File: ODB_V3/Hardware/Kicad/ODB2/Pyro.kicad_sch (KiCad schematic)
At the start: 57 parts, among them J1 1715310000, J7 1715250000, J8 1715310000, J9 1715250000, U11 SI5442DU-T1-GE3, U12 SI5442DU-T1-GE3, U2 LM339, U3 SI5442DU-T1-GE3, U8 SI5442DU-T1-GE3

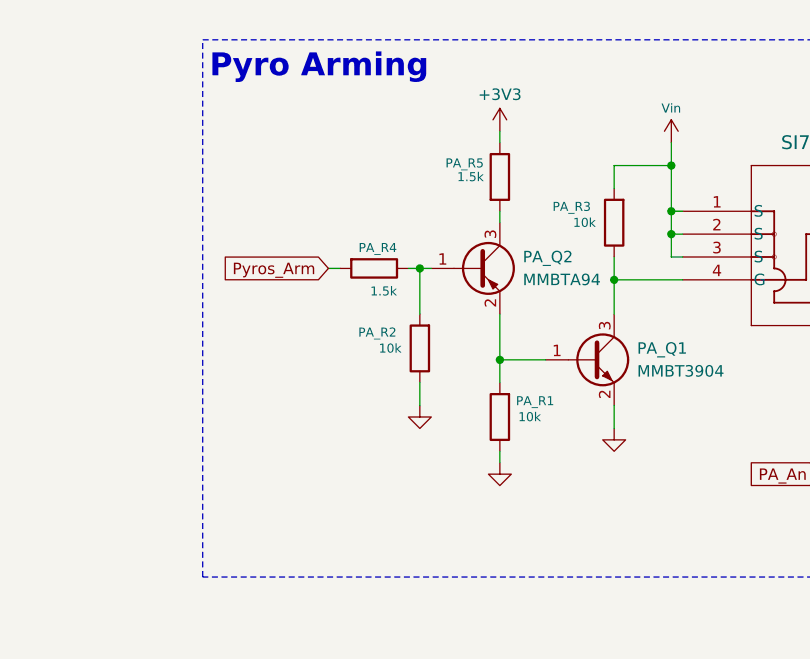
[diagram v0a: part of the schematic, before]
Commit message: WIP : Layout brouillon complet, fix pyro armement
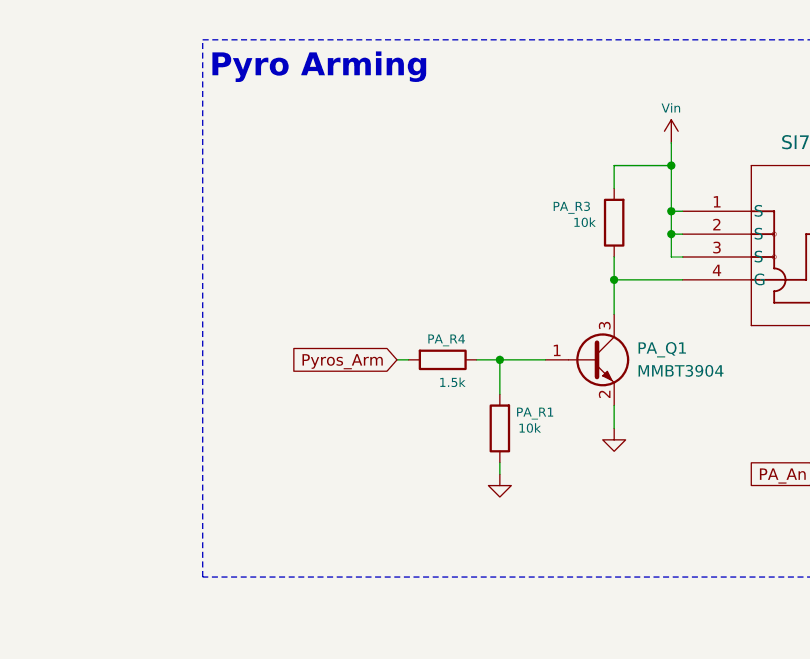
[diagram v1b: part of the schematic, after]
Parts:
- removed PA_Q2: MMBTA94, Package_TO_SOT_SMD:SOT-23, symbol Transistor_BJT:MMBTA94
- removed PA_R2: 10k, Resistor_SMD:R_0603_1608Metric, symbol Device:R
- removed PA_R5: 1.5k, Resistor_SMD:R_0603_1608Metric, symbol Device:R
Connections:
- net at PA_Q1.1 (B), PA_R1.2: now also PA_R4.1
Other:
- moved on the sheet: PA_R1, PA_R4

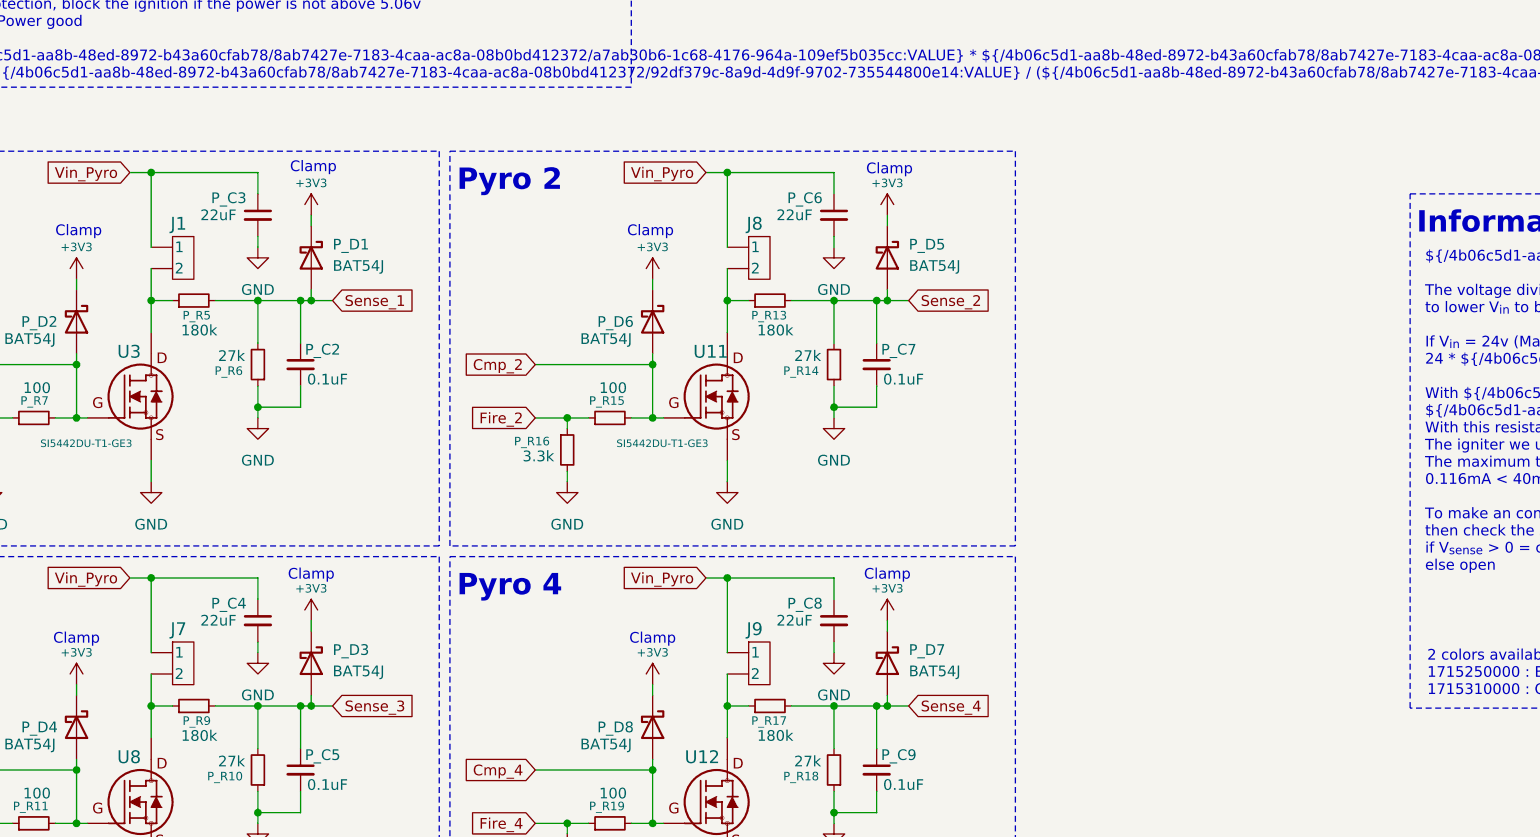
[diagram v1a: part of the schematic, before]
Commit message: WIP : Add GPIO extend, replace 5mm terminal with 2.54mm, densify layout
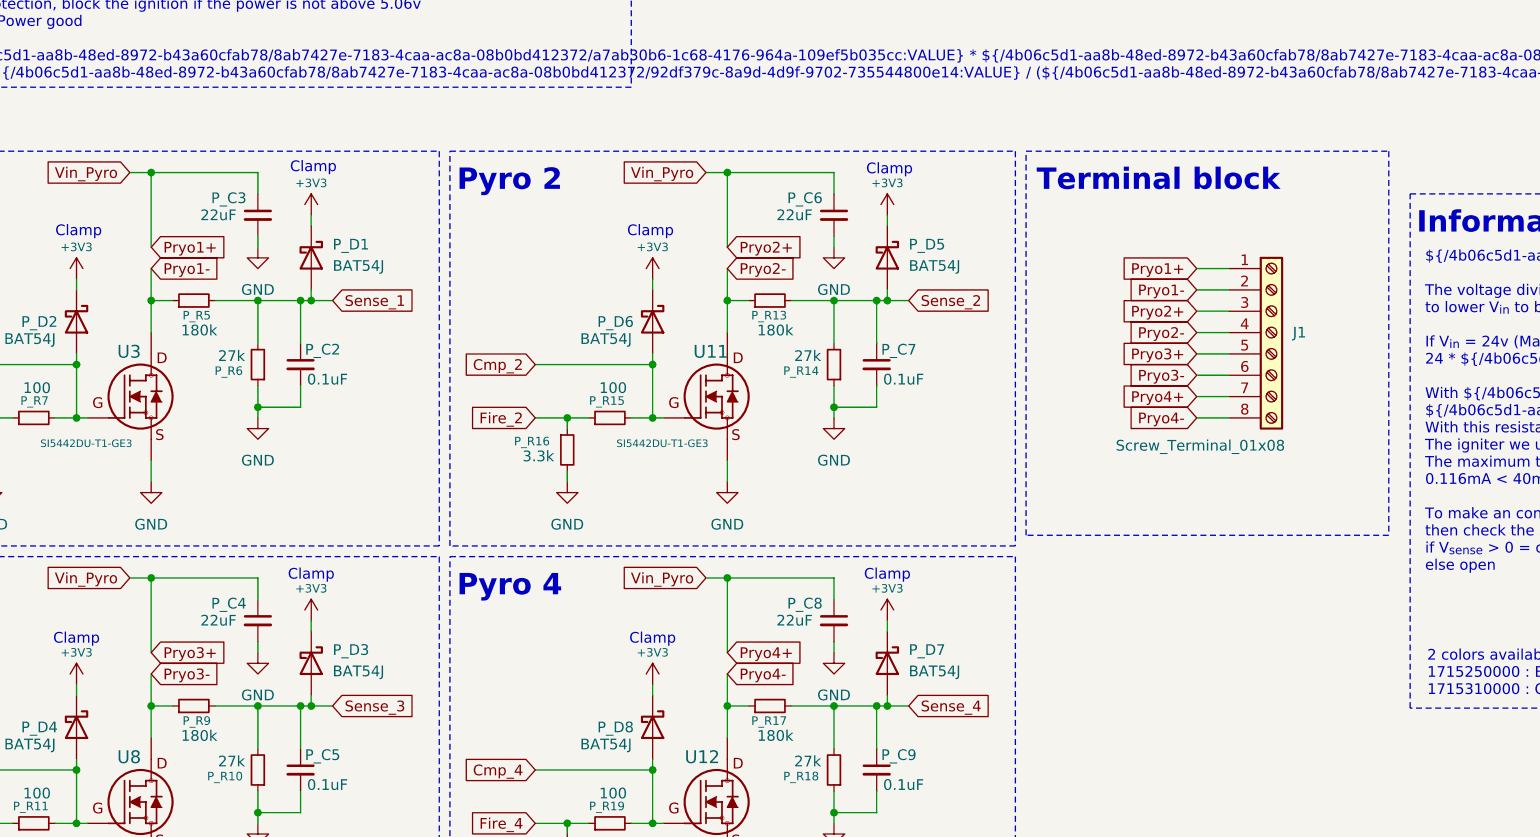
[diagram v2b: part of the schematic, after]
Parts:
- removed J1, J8: 1715310000, ODB:CONN_1715310000, symbol ODB2:1715310000
- removed J7, J9: 1715250000, ODB:CONN_1715310000, symbol ODB2:1715310000
- added J1: Screw_Terminal_01x08, ODB:8pin_terminal_2mm54, symbol Connector:Screw_Terminal_01x08
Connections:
- net Pryo4-: now reaches P_R17.1, U12.1 (D), U12.2 (D), U12.3 (D), U12.6 (D), U12.7 (D), U12.8 (D)
- net Pryo4-: now also J1.8 (Pin_8)
- net Pryo3-: now reaches P_R9.1, U8.1 (D), U8.2 (D), U8.3 (D), U8.6 (D), U8.7 (D), U8.8 (D)
- net Pryo3-: now also J1.6 (Pin_6)
- net Pryo1-: now reaches P_R5.1, U3.1 (D), U3.2 (D), U3.3 (D), U3.6 (D), U3.7 (D), U3.8 (D)
- net Pryo1-: now also J1.2 (Pin_2)
- net Pryo2-: now reaches P_R13.1, U11.1 (D), U11.2 (D), U11.3 (D), U11.6 (D), U11.7 (D), U11.8 (D)
- net Pryo2-: now also J1.4 (Pin_4)
- net Vin_Pyro renamed Pryo1+
- net Pryo1+: now also J1.1 (Pin_1), J1.3 (Pin_3), J1.5 (Pin_5), J1.7 (Pin_7)
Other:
- note added: "Terminal block"

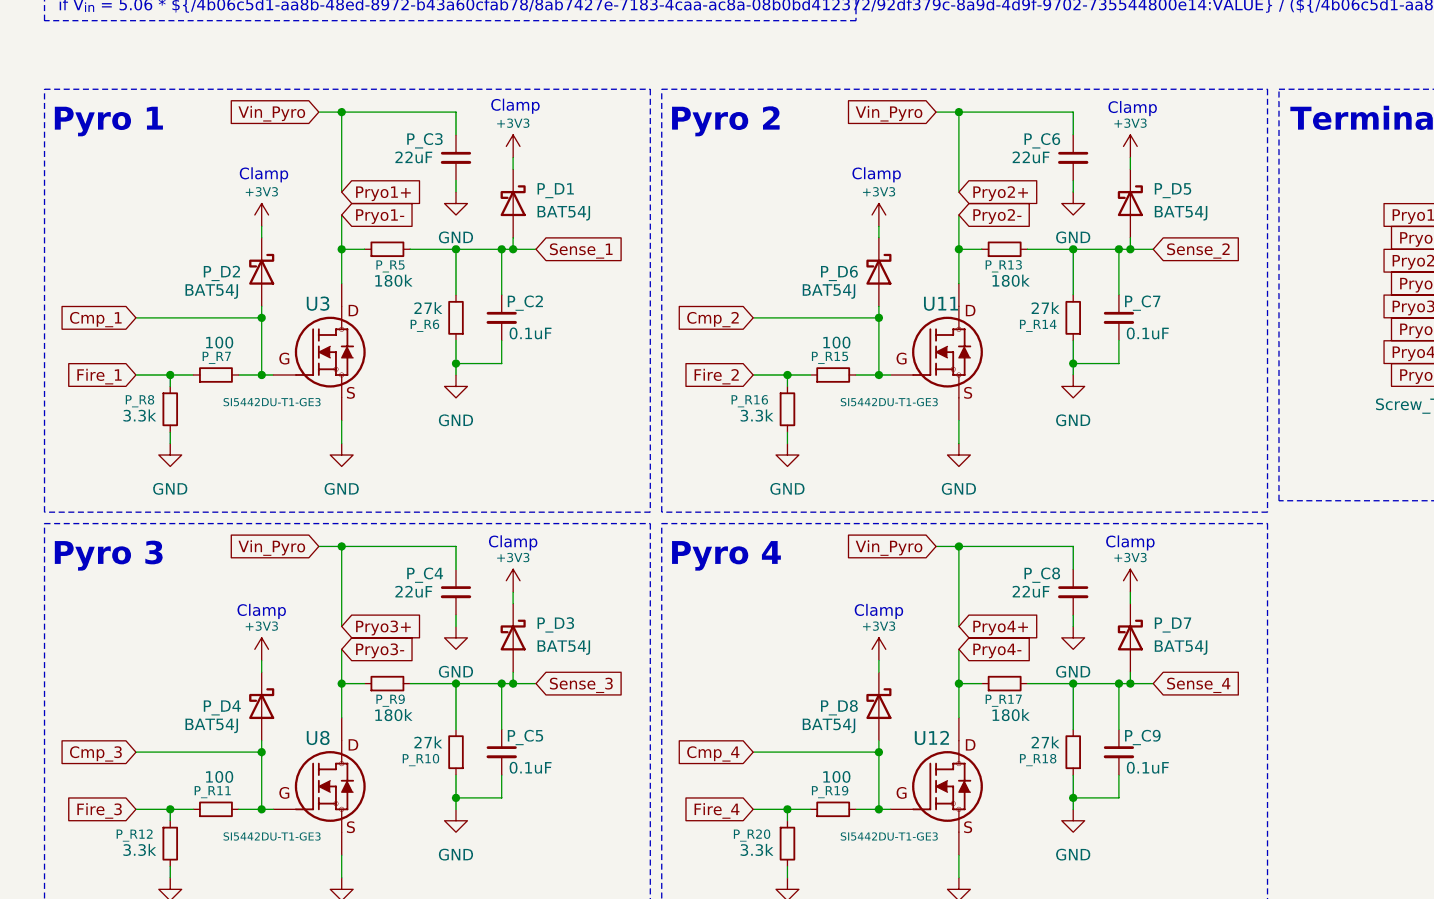
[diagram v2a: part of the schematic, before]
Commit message: fix: reoganised components on pcb
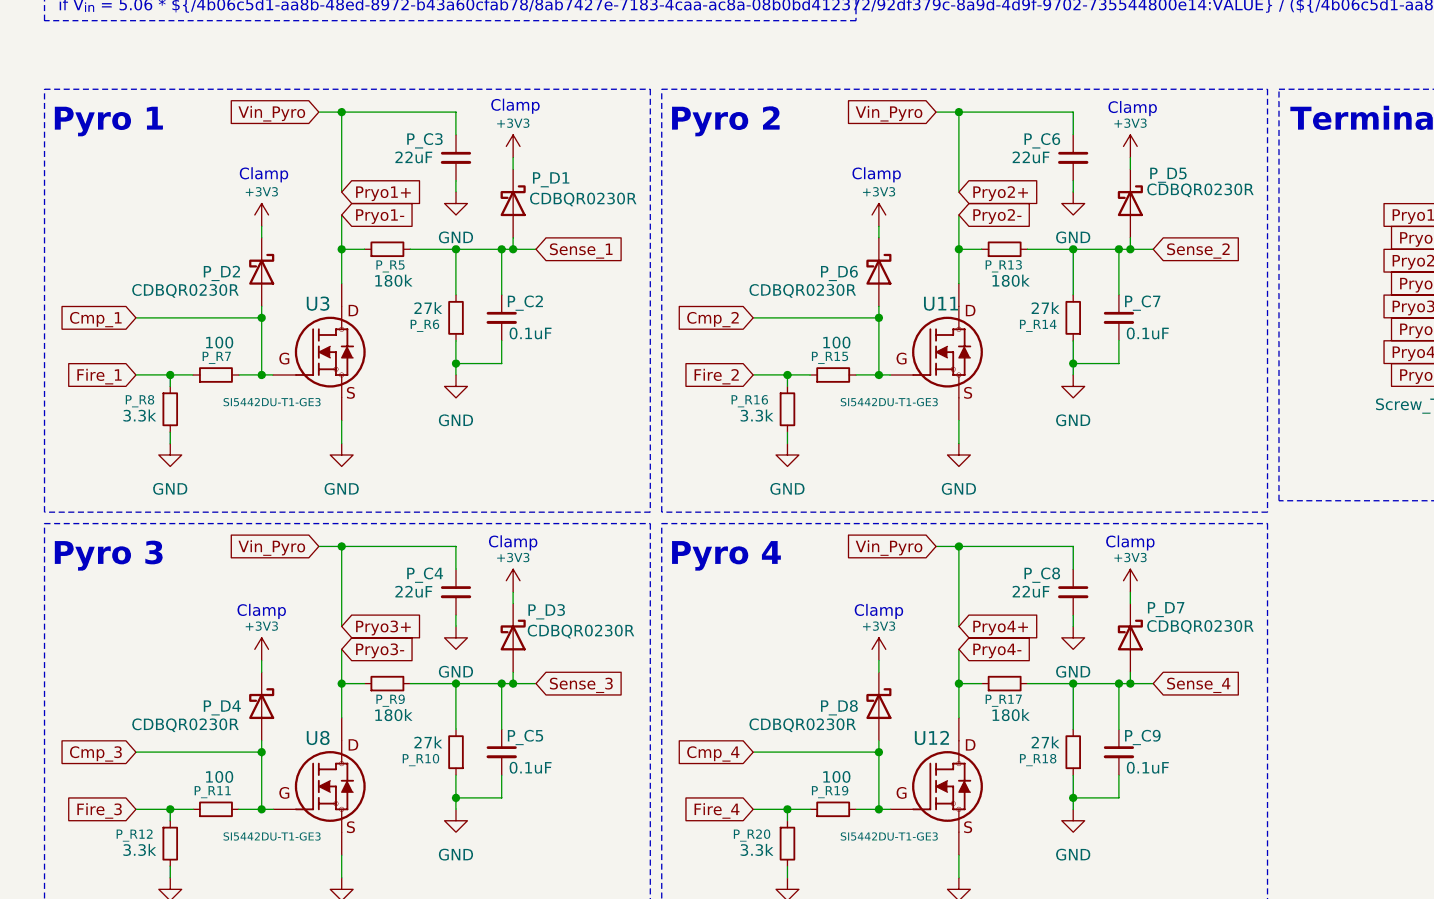
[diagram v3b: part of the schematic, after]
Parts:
- P_D1, P_D2, P_D3, P_D4, P_D5, P_D6, P_D7, P_D8: value BAT54J -> CDBQR0230R; footprint Diode_SMD:D_SOD-323F -> Diode_SMD:D_SOD-923

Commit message: wip: pyro trace
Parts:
- U11, U12, U3, U8: footprint ODB:SON_8DU-T1-GE3_VIS -> SON_8DU-T1-GE3_VIS
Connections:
- net Pryo1+ renamed Pyro1+
- net Pyro1+: now also PA_Q3.9 (D)
- net Pryo1- renamed Pyro1-
- net Pyro1-: now also U3.10 (D)
- net Pryo2- renamed Pyro2-
- net Pyro2-: now also U11.10 (D)
- net Pryo3- renamed Pyro3-
- net Pyro3-: now also U8.10 (D)
- net Pryo4- renamed Pyro4-
- net Pyro4-: now also U12.10 (D)

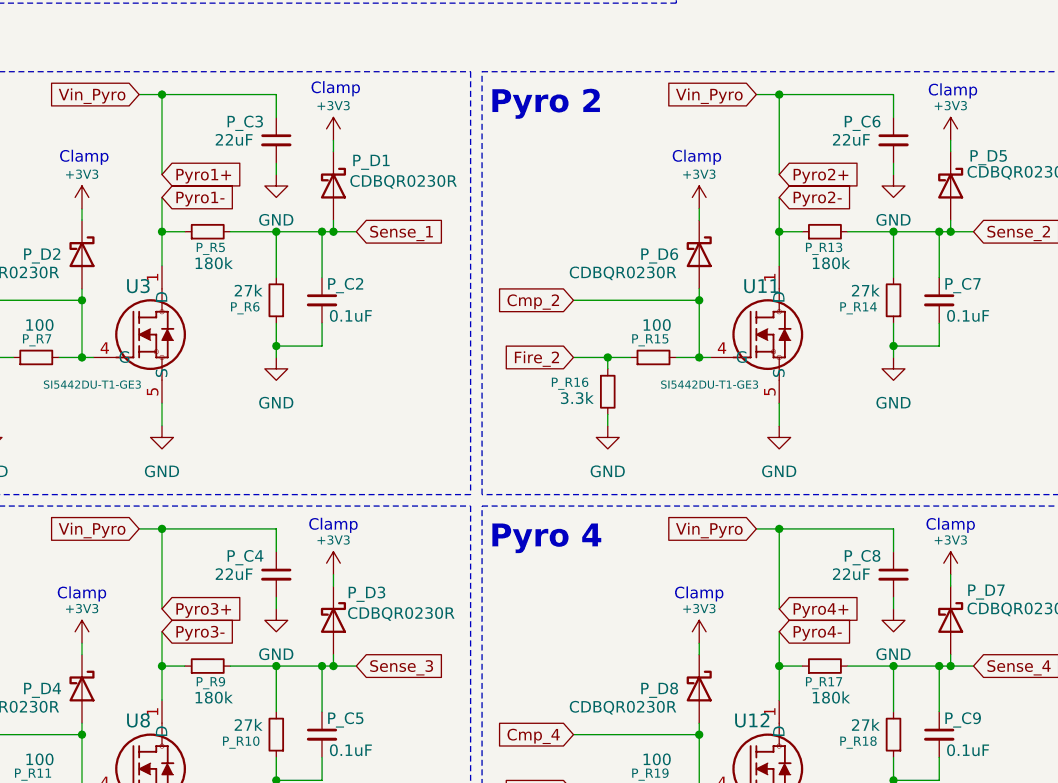
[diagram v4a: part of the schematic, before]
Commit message: wip: add testpads (todo) + add MISO sd resistance + fix pyro labels
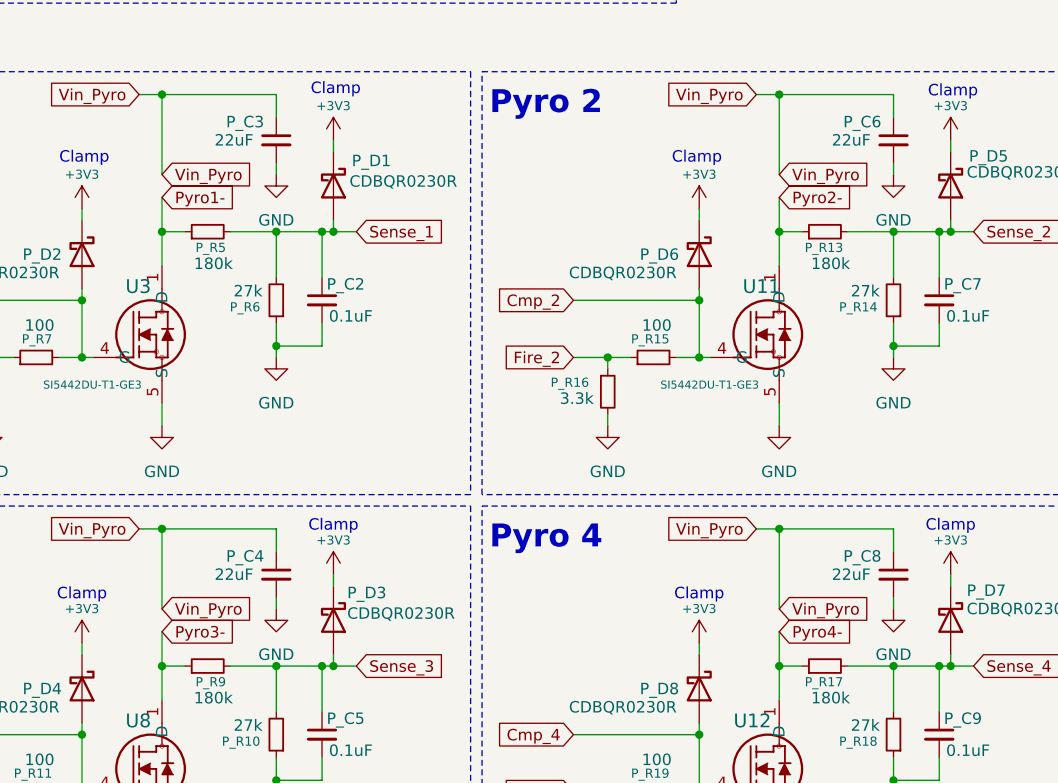
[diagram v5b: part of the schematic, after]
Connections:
- net Pyro1+ renamed Vin_Pyro
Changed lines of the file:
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@@
 		)
 	)
-	(global_label "Pyro1+"
+	(global_label "Vin_Pyro"
 		(shape input)
 		(at 48.26 109.22 0)
@@
 		)
 		(property "Intersheetrefs" "${INTERSHEET_REFS}"
-			(at 58.1999 109.22 0)
+			(at 59.228 109.22 0)
 			(effects
 				(font
@@
 		)
 	)
-	(global_label "Pyro2+"
+	(global_label "Vin_Pyro"
 		(shape input)
 		(at 116.84 109.22 0)
@@
 		)
 		(property "Intersheetrefs" "${INTERSHEET_REFS}"
-			(at 126.7799 109.22 0)
+			(at 127.808 109.22 0)
 			(effects
 				(font
@@
 		)
 	)
-	(global_label "Pyro4+"
+	(global_label "Vin_Pyro"
 		(shape input)
 		(at 116.84 157.48 0)
@@
 		)
 		(property "Intersheetrefs" "${INTERSHEET_REFS}"
-			(at 126.7799 157.48 0)
+			(at 127.808 157.48 0)
 			(effects
 				(font
@@
 		)
 	)
-	(global_label "Pyro3+"
+	(global_label "Vin_Pyro"
 		(shape input)
 		(at 48.26 157.48 0)
@@
 		)
 		(property "Intersheetrefs" "${INTERSHEET_REFS}"
-			(at 58.1999 157.48 0)
-			(effects
-				(font
+			(at 59.228 157.48 0)
+			(effects
+				(font

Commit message: fix : silkscreen DRC completely done
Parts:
- U11, U12, U3, U8: footprint SON_8DU-T1-GE3_VIS -> ODB:SON_8DU-T1-GE3_VIS
